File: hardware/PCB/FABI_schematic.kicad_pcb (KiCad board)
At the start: 2 copper layers, 81 x 55 mm, 51 parts, among them J1 AudioJack3_Ground, J10 Conn_01x03_Male, J11 dispaly_connector_91601-304LF, J11_GND1 Conn_01x01_Male, J11_VDD1 Conn_01x01_Male, J11_data1 Conn_01x01_Male, J2 AudioJack3_Ground, J3 AudioJack3_Ground, J4 AudioJack3_Ground, J5 AudioJack3_Ground, J6 AudioJack3_Ground, J7 AudioJack3_Ground, J8 AudioJack3_Ground, J9 Conn_02x05_Odd_Even, U1 MPXV7007GP, U2 ProMicro

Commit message: Signed-off-by: fussthalerandreas <fussthaler.andreas1997@gmail.com>
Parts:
- R8, R_8: value 150 -> 200
- moved R6 7.75 mm to (96.5, 120.3), turned to 90 degrees
- moved R7 7.75 mm to (99.0, 120.3), turned to 90 degrees
- moved R_6 0.50 mm to (97.7, 117.8), turned to 180 degrees
- moved R_7 0.25 mm to (97.7, 115.6), turned to 180 degrees
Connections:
- R6 pad 1: SDA -> VCC
- R6 pad 2: VCC -> SDA
- R7 pad 1: SCL -> VCC
- R7 pad 2: VCC -> SCL
- R_6 pad 1: SDA -> VCC
- R_6 pad 2: VCC -> SDA
- R_7 pad 1: SCL -> VCC
- R_7 pad 2: VCC -> SCL
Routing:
- net VCC: track 50.5 -> 56.1 mm
- net SCL: track 25.0 -> 24.5 mm

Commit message: Changed power for MPX,Neopixel and Addon from RAW pin to VCC pin, RAW pin is connected via a diode, so ~VUSB-0.6V; VCC is directly connected to VUSB (for 5V version)
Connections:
- J10 pad 1: VDD -> VCC
- J11_VDD1 pad 1: VDD -> VCC
- J9 pad 9: VDD -> VCC
- U2 pad 24: VDD -> Net-(U2-Pad24)
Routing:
- net VDD: track 57.5 -> 0.00 mm
- net VCC: track 56.1 -> 62.6 mm, vias 0 -> 1
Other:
- board text added: "v1.1"

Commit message: Changed buzzer footprint to cheaper, smaller and tone-capable buzzer
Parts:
- J11: value dispaly_connector_91601-304LF -> display_connector_91601-304LF
- bzr1: footprint Buzzer_Beeper:Buzzer_12x9.5RM7.6 -> Buzzer_Beeper:Buzzer_TDK_PS1240P02BT_D12.2mm_H6.5mm
- moved bzr1 1.25 mm to (93.7, 98.3)
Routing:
- net Net-(R8-Pad2): track 7.89 -> 9.45 mm
- net Buzzer_Pin: track 10.7 -> 11.3 mm
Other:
- board text added: "v1.2"
- board text removed: "v1.0"
- board text removed: "v1.1"

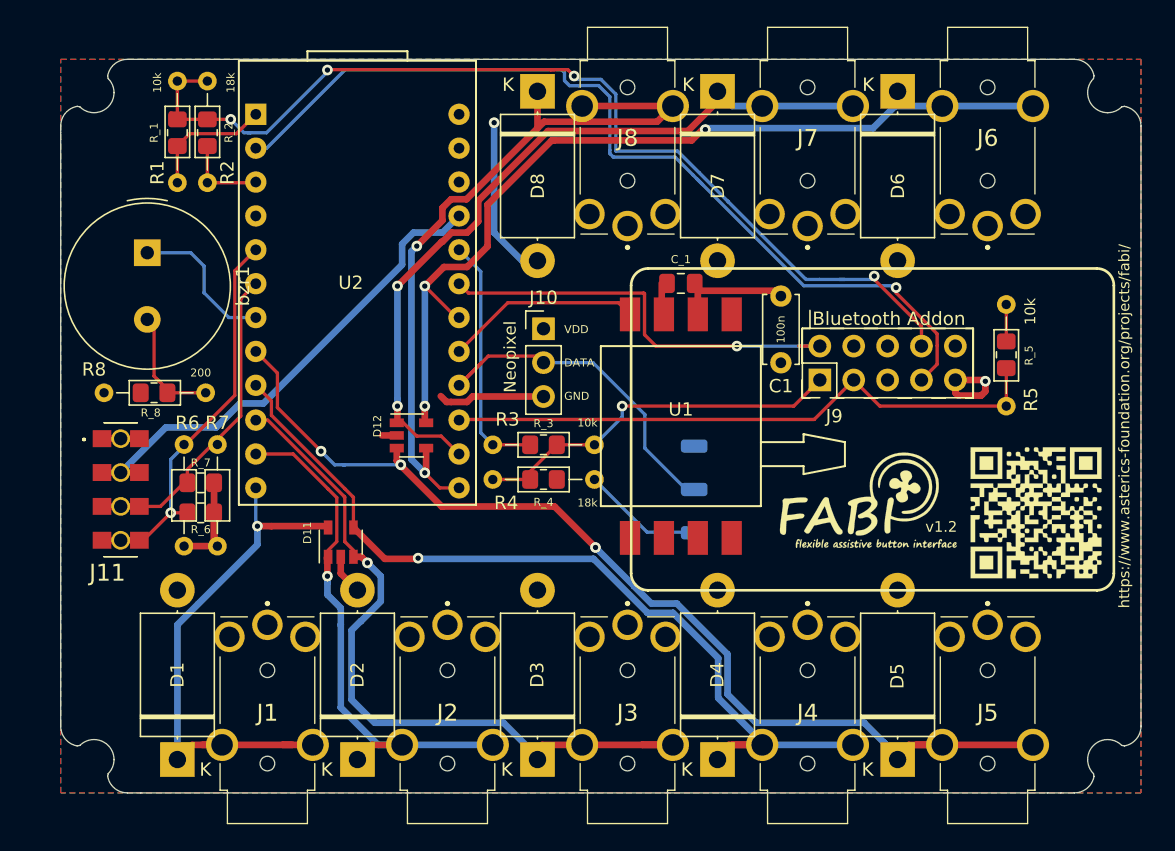
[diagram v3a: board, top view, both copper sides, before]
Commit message: Added GND/VCC planes to PCB & updated to KiCAD 6
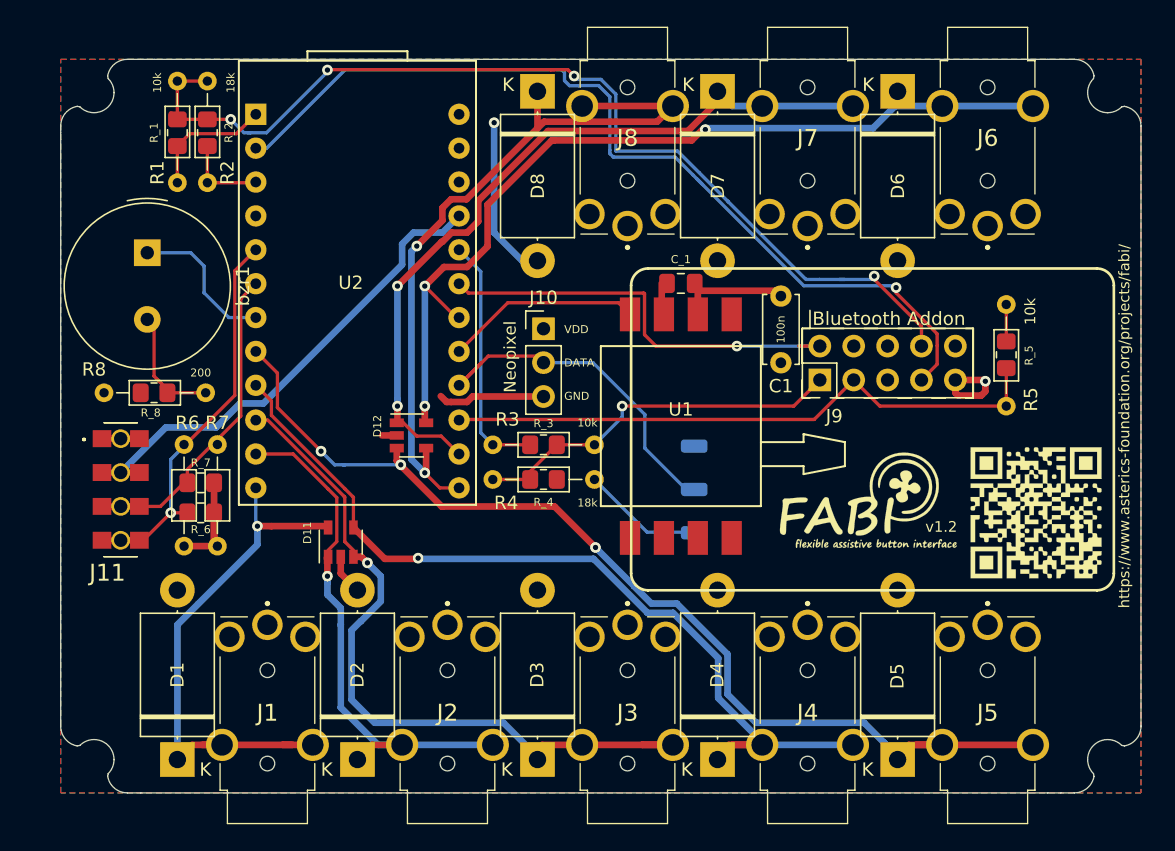
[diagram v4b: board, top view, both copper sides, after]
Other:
- net class Default removed

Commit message: First PCB draft of FABI3
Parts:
- removed C_1: 100n, Capacitor_SMD:C_0805_2012Metric_Pad1.18x1.45mm_HandSolder
- removed D1, D2, D3, D4, D5, D6, D7, D8: P6KE6.8A, Diode_THT:D_DO-201AE_P12.70mm_Horizontal
- removed D11, D12: SP0504BAHT, Package_TO_SOT_SMD:SOT-23-5
- removed G*** (x2): LOGO, FABI_customLibs:QR_FABI_ProjectPage
- removed G***: LOGO, Logos:fabi_15x8
- removed G***: LOGO, FABI_customLibs:FABI_Logo_s
- removed G***: LOGO, FABI_customLibs:FH_logo_m
- removed J7, J8: AudioJack3_Ground, FABI_customLibs:FC68125
- removed REF**: ESP32_Addon, FABI_customLibs:ESP32_Addon
- removed R_1, R_3, R_5, R_6, R_7: 10k, Resistor_SMD:R_0805_2012Metric_Pad1.20x1.40mm_HandSolder
- removed R_2, R_4: 18k, Resistor_SMD:R_0805_2012Metric_Pad1.20x1.40mm_HandSolder
- removed R_8: 200, Resistor_SMD:R_0805_2012Metric_Pad1.20x1.40mm_HandSolder
- removed bzr1: Buzzer, Buzzer_Beeper:Buzzer_TDK_PS1240P02BT_D12.2mm_H6.5mm
- added BZ1: Buzzer, Buzzer_Beeper:Buzzer_TDK_PS1240P02BT_D12.2mm_H6.5mm, F.Cu at (106.6, 88.4)
- added BZ2: PKMCS0909E4000, Buzzer_Beeper:Buzzer_Murata_PKMCS0909E, F.Cu at (106.6, 90.7)
- added C10: 100n, Capacitor_SMD:C_0603_1608Metric, F.Cu at (112.1, 113.7)
- added C11: 100n, Capacitor_SMD:C_0603_1608Metric, F.Cu at (101.7, 113.7)
- added C12: 1uF / >6.3V / X7R, Capacitor_SMD:C_0603_1608Metric, F.Cu at (103.7, 113.7)
- added C2: 100n, Capacitor_SMD:C_0603_1608Metric, F.Cu at (165.3, 91.7)
- added C3: 100n, Capacitor_SMD:C_0603_1608Metric, F.Cu at (128.1, 102.7)
- added C4: 100n, Capacitor_SMD:C_0603_1608Metric, F.Cu at (94.2, 93.6)
- added C8: 100uF/6.3V, Capacitor_SMD:C_1210_3225Metric, F.Cu at (98.1, 125.9)
- added C9: 1uF / >6.3V / X7R, Capacitor_SMD:C_0603_1608Metric, F.Cu at (110.1, 113.7)
- added D10: SFH4045, FLipMouse:SFH4045N, F.Cu at (96.7, 137.3)
- added D13: SFH4045, FLipMouse:SFH4045N, F.Cu at (88.7, 93.3)
- added D14: SFH4045, FLipMouse:SFH4045N, F.Cu at (88.7, 129.3)
- added D15: SFH4045, FLipMouse:SFH4045N, F.Cu at (96.4, 85.3)
- added FID10: Fiducial, Fiducial:Fiducial_0.5mm_Mask1mm, F.Cu at (162.7, 89.3)
- added FID11: Fiducial, Fiducial:Fiducial_0.5mm_Mask1mm, F.Cu at (99.3, 113.7)
- added FID12: Fiducial, Fiducial:Fiducial_0.5mm_Mask1mm, F.Cu at (115.4, 113.7)
- added FID7: Fiducial, Fiducial:Fiducial_0.5mm_Mask1mm, F.Cu at (92.7, 89.3)
- added FID8: Fiducial, Fiducial:Fiducial_0.5mm_Mask1mm, F.Cu at (92.7, 133.3)
- added FID9: Fiducial, Fiducial:Fiducial_0.5mm_Mask1mm, F.Cu at (162.7, 133.3)
- added J12: 009159005551906, FLipMouse:009159005551906, F.Cu at (131.9, 116.5)
- added J13: Conn_01x04_Male, FLipMouse:pressure_sensor, F.Cu at (105.3, 121.0)
- added JP5: SolderJumper_2_Bridged, Jumper:SolderJumper-2_P1.3mm_Bridged_RoundedPad1.0x1.5mm, F.Cu at (93.5, 128.7)
- added JP6: SolderJumper_2_Bridged, Jumper:SolderJumper-2_P1.3mm_Bridged_RoundedPad1.0x1.5mm, F.Cu at (93.5, 126.0)
- added LOGO5: Logo_FABI, FABI:FABI_Logo_s, B.Cu at (152.1, 94.6)
- added LOGO6: Logo_KiCAD, Symbol:KiCad-Logo_5mm_SilkScreen, B.Cu at (119.7, 118.0)
- added LOGO7: Logo_CE, Symbol:CE-Logo_8.5x6mm_SilkScreen, B.Cu at (147.5, 128.3)
- added LOGO8: Logo_WEEE, Symbol:WEEE-Logo_5.6x8mm_SilkScreen, B.Cu at (155.3, 127.8)
- added NT1: NetTie_2, NetTie:NetTie-2_SMD_Pad0.5mm, F.Cu at (164.5, 103.2)
- added NT2: NetTie_2, NetTie:NetTie-2_SMD_Pad0.5mm, F.Cu at (113.9, 112.9)
- added Q1: BSS806, Package_TO_SOT_SMD:SOT-23, F.Cu at (97.5, 131.3)
- added R9: 4k7, Resistor_SMD:R_0603_1608Metric, F.Cu at (97.4, 133.9)
- added TP1: TestPoint, TestPoint:TestPoint_Pad_D1.0mm, F.Cu at (163.0, 103.2)
- added U3: TSOP4838, OptoDevice:Vishay_MOLD-3Pin, F.Cu at (163.4, 128.9)
- added U4: TPD3E001DRLR, Package_TO_SOT_SMD:SOT-553, F.Cu at (120.2, 120.5)
- added U5: MIC5504-3.3YM5, Package_TO_SOT_SMD:SOT-23-5, F.Cu at (106.9, 113.7)
- added U6: TPD3E001DRLR, Package_TO_SOT_SMD:SOT-553, F.Cu at (163.3, 91.6)
- added U7: TPD3E001DRLR, Package_TO_SOT_SMD:SOT-553, F.Cu at (128.1, 100.5)
- C1: footprint Capacitor_THT:C_Disc_D5.0mm_W2.5mm_P5.00mm -> Capacitor_SMD:C_0603_1608Metric
- J1, J2, J3, J4, J5, J6: footprint FABI_customLibs:FC68125 -> FABI:FC68125
- J11: footprint FABI_customLibs:91601304LF -> FABI:91601304LF
- J9: value Conn_02x05_Odd_Even -> Conn_ARM_SWD_TagConnect_TC2030; footprint Connector_PinHeader_2.54mm:PinHeader_2x05_P2.54mm_Vertical -> Connector:Tag-Connect_TC2030-IDC-FP_2x03_P1.27mm_Vertical
- R1: value 10k -> 4k7; footprint Resistor_THT:R_Axial_DIN0204_L3.6mm_D1.6mm_P7.62mm_Horizontal -> Resistor_SMD:R_0603_1608Metric
- R2: value 18k -> 4k7; footprint Resistor_THT:R_Axial_DIN0204_L3.6mm_D1.6mm_P7.62mm_Horizontal -> Resistor_SMD:R_0603_1608Metric
- R3: value 10k -> 200; footprint Resistor_THT:R_Axial_DIN0204_L3.6mm_D1.6mm_P7.62mm_Horizontal -> Resistor_SMD:R_0805_2012Metric_Pad1.20x1.40mm_HandSolder
- R4: value 18k -> DNP; footprint Resistor_THT:R_Axial_DIN0204_L3.6mm_D1.6mm_P7.62mm_Horizontal -> Resistor_SMD:R_0603_1608Metric
- R5: value 10k -> DNP; footprint Resistor_THT:R_Axial_DIN0204_L3.6mm_D1.6mm_P7.62mm_Horizontal -> Resistor_SMD:R_0603_1608Metric
- U1: value MPXV7007GP -> RaspberryPi_Pico_W_SecondaryPins; footprint MPXV7007GP:MPXV7007GP -> Module_RaspberryPi_Pico:RaspberryPi_Pico_W_SMD
- U2: value ProMicro -> TPD3E001DRLR; footprint FABI_customLibs:ProMicro -> Package_TO_SOT_SMD:SOT-553
- moved R2 74.0 mm to (166.1, 114.9), turned to 90 degrees
- moved R1 71.1 mm to (163.6, 114.9)
- moved R6 70.2 mm to (166.1, 111.1), turned to -90 degrees
- moved R5 66.1 mm to (93.5, 123.9), turned to 0 degrees
- moved R7 65.3 mm to (163.6, 111.1), turned to -90 degrees
- moved J6 65.1 mm to (93.0, 103.3), turned to 90 degrees
- moved J5 57.1 mm to (119.2, 89.8), turned to 0 degrees
- moved J4 44.3 mm to (132.7, 89.8), turned to 0 degrees
- moved R4 30.4 mm to (93.5, 130.9)
- moved C1 29.6 mm to (120.3, 122.5), turned to 180 degrees
- moved R3 29.4 mm to (98.6, 92.3), turned to 90 degrees
- moved U1 16.5 mm to (150.1, 109.6), turned to 0 degrees
- moved U2 16.0 mm to (94.2, 95.8)
- moved R8 15.1 mm to (98.6, 96.1), turned to 90 degrees
- moved J9 10.8 mm to (134.0, 104.4), turned to 0 degrees
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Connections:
- J1 pad 2R: Net-(J1-Pad2R) -> unconnected-(J1-Pad2R)
- J1 pad 3T: AUX_1 -> /BUTTON1
- J1 pad 6SR: Net-(J1-Pad6SR) -> unconnected-(J1-Pad6SR)
- J10 pad 1: VCC -> VBUS
- J10 pad 2: NEOPIXEL -> /NEOPIXEL
- J11 pad 5: SCL -> /SCL_INT
- J11 pad 7: SDA -> /SDA_INT
- J11_VDD1 pad 1: VCC -> VBUS
- J11_data1 pad 1: NEOPIXEL -> /NEOPIXEL
- J2 pad 2R: Net-(J2-Pad2R) -> unconnected-(J2-Pad2R)
- J2 pad 3T: AUX_2 -> /BUTTON2
- J2 pad 6SR: Net-(J2-Pad6SR) -> unconnected-(J2-Pad6SR)
- J3 pad 2R: Net-(J3-Pad2R) -> unconnected-(J3-Pad2R)
- J3 pad 3T: AUX_3 -> /BUTTON3
- J3 pad 6SR: Net-(J3-Pad6SR) -> unconnected-(J3-Pad6SR)
- J4 pad 2R: Net-(J4-Pad2R) -> unconnected-(J4-Pad2R)
- J4 pad 3T: AUX_4 -> /BUTTON4
- J4 pad 6SR: Net-(J4-Pad6SR) -> unconnected-(J4-Pad6SR)
- J5 pad 2R: Net-(J5-Pad2R) -> unconnected-(J5-Pad2R)
- J5 pad 3T: AUX_5 -> /BUTTON5
- J5 pad 6SR: Net-(J5-Pad6SR) -> unconnected-(J5-Pad6SR)
- J6 pad 1S: GND -> GNDA
- J6 pad 2R: Net-(J6-Pad2R) -> /SCL
- J6 pad 3T: AUX_6 -> +3.3VADC
- J6 pad 6SR: Net-(J6-Pad6SR) -> /SDA
- J9 pad 1: ESP_AddOn_Pin1 -> VCC
- J9 pad 2: AddOn_Pin2 -> Net-(J9-SWDIO)
- J9 pad 3: AddOn_Pin3 -> /RESET
- J9 pad 4: Net-(J9-Pad4) -> Net-(J9-SWCLK)
- J9 pad 5: Net-(J9-Pad5) -> GND
- J9 pad 6: GND -> unconnected-(J9-SWO-Pad6)
- R1 pad 1: A_TX -> /SCL_INT
- R1 pad 2: ESP_RX -> VCC
- R2 pad 1: ESP_RX -> /SDA_INT
- R2 pad 2: GND -> VCC
- R3 pad 1: AddOn_Pin1 -> GND
- R3 pad 2: ESP_AddOn_Pin1 -> Net-(BZ1-+)
- R4 pad 1: ESP_AddOn_Pin1 -> Net-(D10-A)
- R4 pad 2: GND -> VCC
- R5 pad 1: AddOn_Pin3 -> Net-(D13-A)
- R5 pad 2: GND -> VCC
- R6 pad 2: SDA -> /SDA_INT
- R7 pad 2: SCL -> /SCL_INT
- R8 pad 2: Net-(R8-Pad2) -> Net-(BZ1-+)
- U1 pad 1: Net-(U1-Pad1) -> unconnected-(U1-GPIO0-Pad1)
- U1 pad 2: VCC -> unconnected-(U1-GPIO1-Pad2)
- U1 pad 4: MPX -> /BUZZER
- U1 pad 5: Net-(U1-Pad5) -> /BUTTON4
- U1 pad 6: Net-(U1-Pad6) -> /BUTTON5
- U1 pad 7: Net-(U1-Pad7) -> /MPRLS_DRDY_RES
- U1 pad 8: Net-(U1-Pad8) -> GND
- U2 pad 1: A_TX -> unconnected-(U2-IO1-Pad1)
- U2 pad 2: A_RX -> /SDA
- U2 pad 3: GND -> GNDA
- U2 pad 4: GND -> /SCL
- U2 pad 5: SDA -> +3.3VADC
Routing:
- net VCC: track 62.6 -> 213.4 mm, vias 1 -> 5
- net /SCL_INT: track 0.00 -> 105.7 mm, vias 0 -> 4
- net VBUS: track 0.00 -> 101.4 mm, vias 0 -> 2
- net /SDA_INT: track 0.00 -> 100.1 mm, vias 0 -> 2
- net /SDA: track 0.00 -> 87.5 mm, vias 0 -> 2
- net GND: track 50.1 -> 136.9 mm, vias 1 -> 15
- net /SCL: track 0.00 -> 82.7 mm, vias 0 -> 4
- net AUX_5: track 80.7 -> 0.00 mm, vias 3 -> 0
- net ESP_RX: track 78.4 -> 0.00 mm, vias 4 -> 0
- net +3.3VADC: track 0.00 -> 75.2 mm, vias 0 -> 5
- net A_RX: track 69.6 -> 0.00 mm, vias 1 -> 0
- net GNDA: track 0.00 -> 69.0 mm
- net AUX_6: track 68.4 -> 0.00 mm, vias 3 -> 0
- net AUX_4: track 67.7 -> 0.00 mm, vias 1 -> 0
- net Net-(D14-K): track 0.00 -> 62.9 mm
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- added copper zone on B.Cu, net GND
- removed copper zone on B.Cu, net VCC
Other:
- board text added: "+5V"
- board text added: "FABI - Flexible Assistive Button Interface AsTeRICS Foundation / UAS Technikum Wien office@asterics-foundation.org Benjamin Aigner"
- board text added: "https://www.asterics-foundation.org/projects/fabi/ https://github.com/asterics/fabi"
- board text added: "v3.0"
- board text removed: "Bluetooth Addon"
- board text removed: "FABI - Flexible Assistive Button Interface AsTeRICS Foundation / UAS Technikum Wien office@asterics-foundation.org Benjamin Aigner, Andreas Fußthaler, Christoph Veigl"
- board text removed: "https://www.asterics-foundation.org/projects/fabi/"
- board text removed: "v1.2"

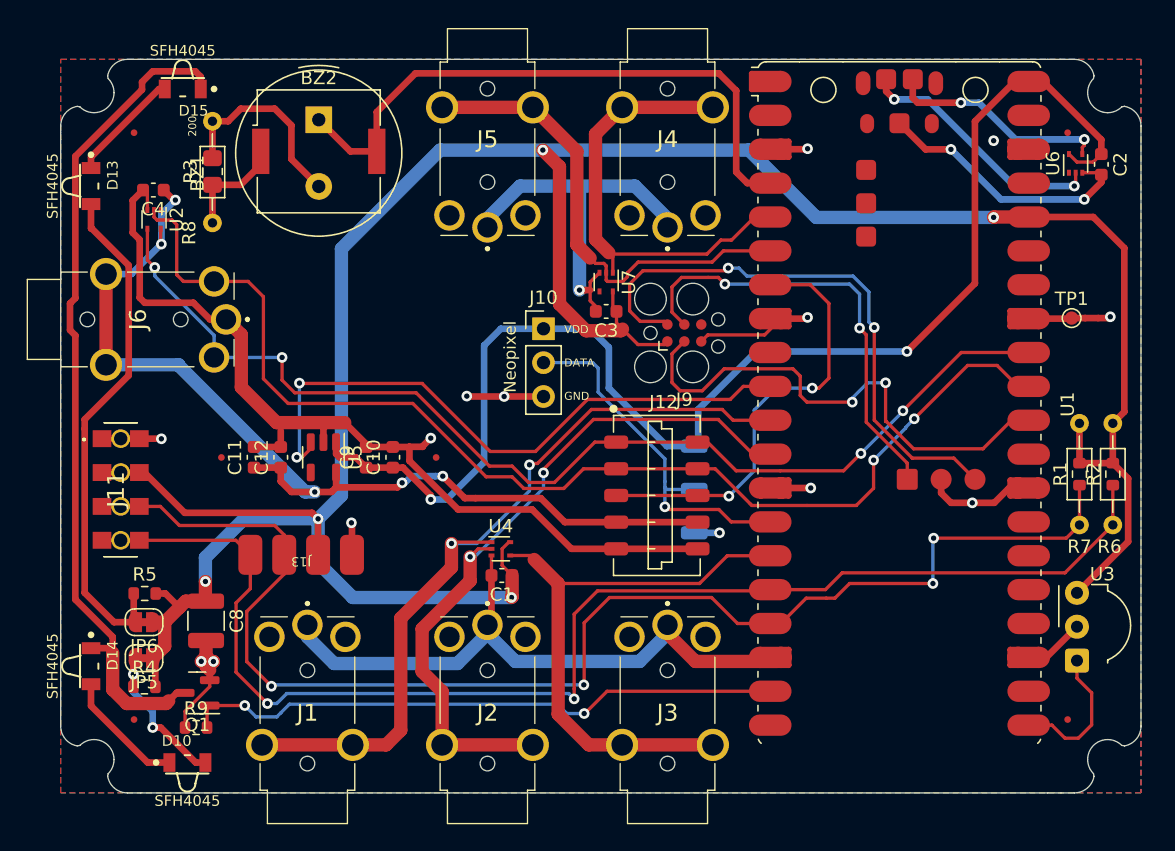
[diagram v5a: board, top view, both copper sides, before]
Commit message: silkscreen changes
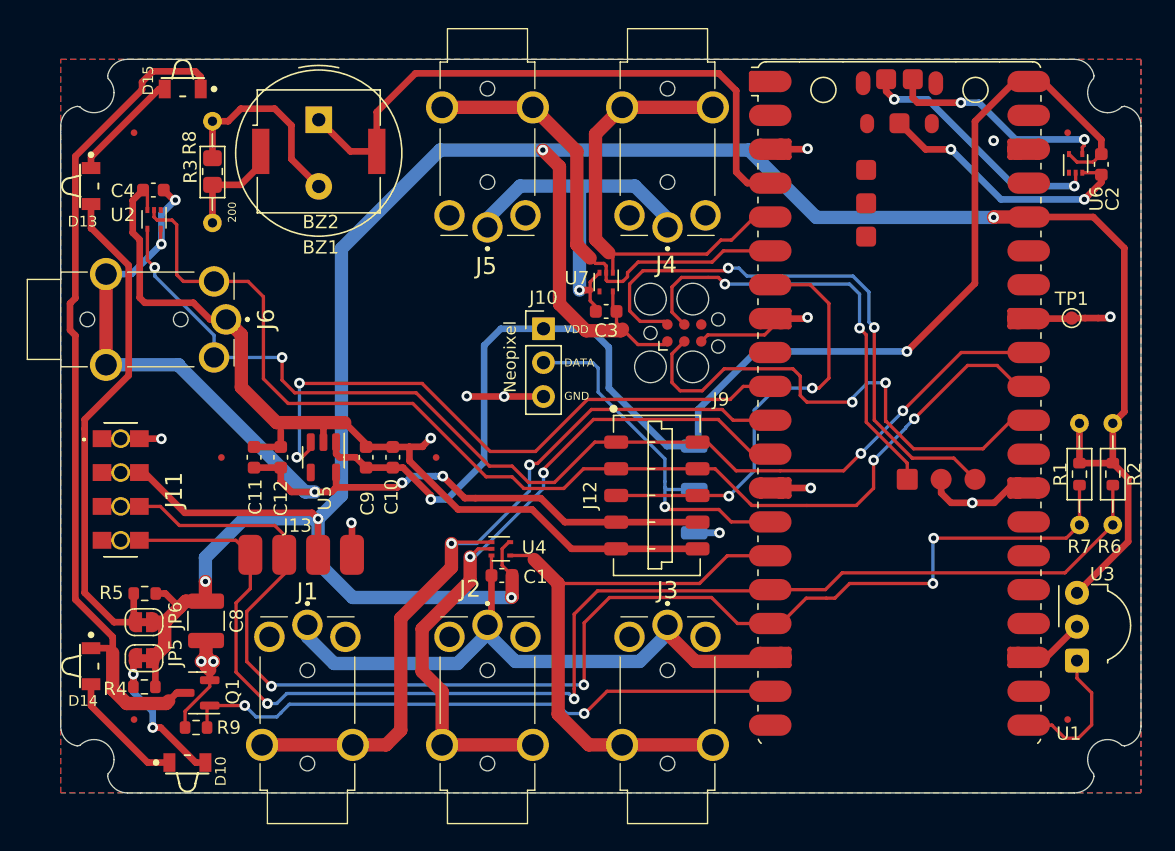
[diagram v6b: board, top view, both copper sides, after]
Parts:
- moved LOGO6 42.0 mm to (151.9, 91.0)
- moved LOGO5 38.1 mm to (114.2, 99.2)
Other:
- board text added: "DIN"

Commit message: Updated PCB to move MPRLS connector away from PicoW; rerouted and exported STEP
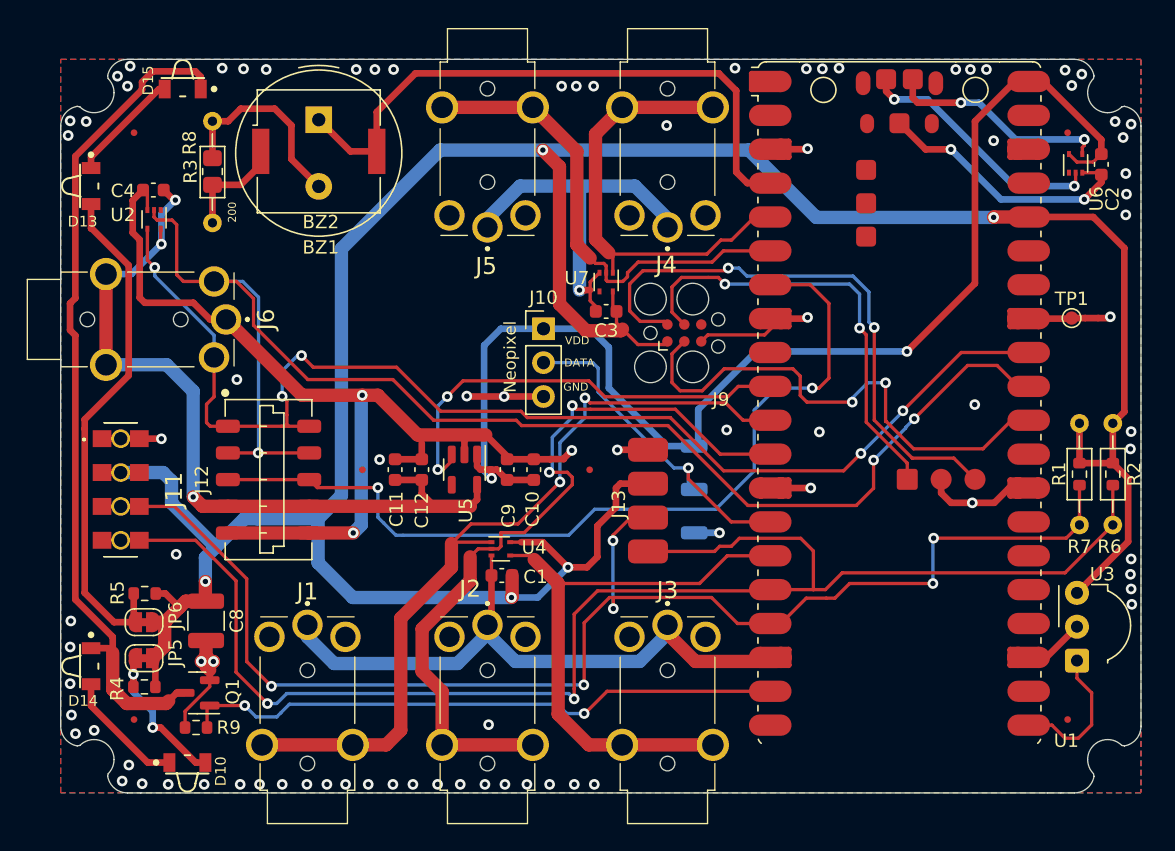
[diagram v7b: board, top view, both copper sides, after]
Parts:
- moved J12 29.1 mm to (102.8, 115.3)
- moved J13 26.3 mm to (131.3, 116.9), turned to -90 degrees
- moved FID12 11.5 mm to (126.9, 114.6)
- moved C10 10.6 mm to (122.7, 114.6)
- moved C11 10.6 mm to (112.3, 114.6)
- moved C12 10.6 mm to (114.3, 114.6)
- moved C9 10.6 mm to (120.7, 114.6)
- moved NT2 10.6 mm to (124.5, 113.8)
- moved U5 10.6 mm to (117.5, 114.6)
- moved FID11 10.6 mm to (109.9, 114.6)
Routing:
- net /MPRLS_DRDY_RES: track 32.1 -> 65.4 mm
- net /SDA: track 87.5 -> 105.5 mm, vias 2 -> 3
- net /SDA_INT: track 100.1 -> 115.0 mm
- net /3V3_ADC_ENABLE: track 47.7 -> 33.9 mm
- net +3.3VADC: track 75.2 -> 62.1 mm, vias 5 -> 3
- net VCC: track 213.4 -> 224.1 mm
- net /SCL: track 82.7 -> 91.9 mm, vias 4 -> 5
- net VBUS: track 101.4 -> 94.3 mm
- net /BUTTON2: track 54.3 -> 58.8 mm
- net GNDA: track 69.0 -> 72.3 mm, vias 0 -> 2
- net /SCL_INT: track 105.7 -> 107.9 mm, vias 4 -> 6
- net /BUTTON1: track 59.8 -> 62.0 mm
- net /NEOPIXEL: track 28.2 -> 26.1 mm
- net GND: track 136.9 -> 136.8 mm, vias 15 -> 88
